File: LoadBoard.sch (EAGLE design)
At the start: 76 parts, among them IC1 7805TV, IC2 LM358D, IC3 MCP23S17SO, Q1 IRFZ44N, Q2 16MHz, T1 BC817, U1 ATMEGA328P_TQFP, U2 MAX232SOIC16

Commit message: Added second MosFET Stage and Temperature  Sensing
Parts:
- added ENCODER, JP3: (no value), SparkFun-Connectors:M04POLAR
- added FAN_CTRL, VLOAD_ATT: TPB1,27, testpad:TPB1,27
- added H5, H6: 3MM, holes:MOUNT-PAD-ROUND3.0
- added KK3: SK104-PAD, heatsink:SK104-PAD
- added LED1, LED2: (no value), led:LEDB155
- added Q3: IRFZ44N, OwnStuff:IRFZ44N
- added R14, R15, R16: 100, rcl:R-EU_R1206
- added R17, R18: 4k7, rcl:R-EU_M1206
- added RST_EN: (no value), pinhead:PINHD-1X2
- added U$7, U$8: DS18B20, OwnStuff:DS18B20
- KK1: value SK129 -> SK104-PAD; device heatsink:SK129 -> heatsink:SK104-PAD
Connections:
- new net GNDIO: JP3.1, S1.C, S1.SW-
- new net LED1: R14.1, U1.PC4(ADC4/SDA)
- new net LED2: R15.1, U1.PC5(ADC5/SCL)
- new net N$43: LED1.A, R14.2
- new net N$44: LED2.A, R15.2
- new net N$45: JP3.4, S1.SW+
- new net N$46: JP3.3, S1.A
- new net N$47: Q3.G, R16.2
- new net N$49: JP3.2, S1.B
- new net RST_EN: C12.2, RST_EN.1
- new net TH1: R18.2, U$7.DQ, U1.PC0(ADC0)
- new net TH2: R17.2, U$8.DQ, U1.PC1(ADC1)
- net +12V: now also FAN.2; no longer FAN.1
- net BTN_A: now also U1.PD4(XCK/T0); no longer U1.PD3(INT1)
- net BTN_B: now also U1.PD3(INT1); no longer U1.PD4(XCK/T0)
- net ENC_A: now also ENCODER.3; no longer S1.A
- net ENC_B: now also ENCODER.2; no longer S1.B
- net ENC_BTN: now also ENCODER.4; no longer S1.SW+
- net FAN: now also FAN_CTRL.TP
- net GND: now also ENCODER.1, LED1.C, LED2.C, U$7.GND, U$8.GND; no longer S1.C, S1.SW-
- net LOAD+: now also Q3.D
- net N$10: now also R16.1
- net N$12: now also DTR_IN.TP; no longer RX_IN.TP
- net N$13: now also RX_IN.TP; no longer DTR_IN.TP
- net N$26: now also PWR_SWITCH.2; no longer PWR_SWITCH.1
- net N$35: now also U$6.CS2; no longer U$6.DI
- net N$36: now also U$6.CS1; no longer U$6.RW
- net N$38: now also U$6.RW; no longer U$6.CS1
- net N$39: now also U$6.DI; no longer U$6.CS2
- net N$41: now also PWR_SWITCH.1; no longer PWR_SWITCH.2
- net N$5: now also FAN.1; no longer FAN.2
- net N$7: now also RST_EN.2; no longer C12.2
- net VCC: now also R17.1, R18.1, U$7.VDD, U$8.VDD
- net VLOAD_ATT: now also VLOAD_ATT.TP
- net VLOAD_DROP: now also Q3.S, U1.PC2(ADC2)
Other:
- moved on the sheet: C12, C14, C15, C16, C17, C18, C6, C7, DTR_IN, FAN, KK2, Q2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

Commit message: added second fan controller
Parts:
- removed FAN: (no value), SparkFun-Connectors:M02POLAR
- removed FAN_CTRL: TPB1,27, testpad:TPB1,27
- added D3: BAS16J, diode:DIODE-SOD323-W
- added FAN1, FAN2: TPB1,27, testpad:TPB1,27
- added FAN1_CONN, FAN2_CONN: (no value), SparkFun-Connectors:M02POLAR
- added R19: 100, rcl:R-EU_R1206
- added T2: BC817, transistor:BC817-NPN-SOT23-BEC
- added U$10: LM2569, OwnStuff:LM2569
- added U$9: IRLML2502, GeekAmmo:N-CHANNEL-MOSFET-BSS138
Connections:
- removed net FAN: FAN_CTRL.TP, R6.1, U1.PD2(INT0)
- new net FAN1: FAN1.TP, R6.1, U1.PD2(INT0)
- new net FAN2: FAN2.TP, R19.1, U1.PB0(ICP)
- new net N$42: T2.E, U$9.G
- new net N$48: R19.2, T2.B
- new net N$50: D3.A, FAN2_CONN.1, U$9.D
- net +12V: now also D3.C, FAN1_CONN.2, FAN2_CONN.2, T1.C, T2.C, U$10.IN+; no longer FAN.2
- net GND: now also U$10.IN-, U$10.OUT-, U$9.S
- net N$5: now also FAN1_CONN.1; no longer FAN.1, T1.C
- net VCC: now also U$10.OUT+
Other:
- note added: "Encoder Riser Board & Input"
- note added: "Frontpanel I/O"
- note added: "Optional LM2569 Equip EITHER with 7805 OR LM2569"
- note added: "Temperature Sensing"
- note removed: "Input"
- moved on the sheet: +12V, +5V, C1, C14, C15, C16, C17, C18, C2, C3, C4, C5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

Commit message: worked on silkscreen for passives
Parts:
- C3: value 24µ -> 100µ; device rcl:CPOL-EU150CLZ-0810 -> rcl:CPOL-EU175TMP-0808
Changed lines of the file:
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@@
 <part name="C1" library="rcl" deviceset="C-EU" device="C1206K" value="100n"/>
 <part name="C2" library="rcl" deviceset="C-EU" device="C1206K" value="100n"/>
-<part name="C3" library="rcl" deviceset="CPOL-EU" device="150CLZ-0810" value="24µ"/>
+<part name="C3" library="rcl" deviceset="CPOL-EU" device="175TMP-0808" value="100µ"/>
 <part name="GND2" library="supply1" deviceset="GND" device=""/>
 <part name="P+4" library="supply1" deviceset="VCC" device=""/>

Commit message: added silkscreen information to bottom
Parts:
- removed PWR: BLUE, SparkFun-LED:LED0603
- removed U$7, U$8: DS18B20, OwnStuff:DS18B20
- added IC8, IC9: DS18B20, OwnStuff:DS18B20
- added LED3: (no value), led:LEDB155
- added LED4: BLUE, SparkFun-LED:LED0603
- added R20: 100, rcl:R-EU_R1206
- Q1, Q3: value IRFZ44N -> IRF3710
- U$10: value LM2569 -> LM2569NO_OUTLINE; device OwnStuff:LM2569 -> OwnStuff:LM2569NO_OUTLINE
- renumbered ENCODER to JP4, RST_EN to JP5, RXI to LED5, TXI to LED6, U$1 to IC6, U$2 to IC7, U$4 to U4, U$9 to U9, U1 to IC4, U2 to IC5
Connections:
- new net N$51: LED3.A, R20.2
- net GND: now also IC8.GND, IC9.GND, LED3.C, LED4.C; no longer PWR.C, U$7.GND, U$8.GND
- net N$20: now also LED4.A; no longer PWR.A
- net TH1: now also IC8.DQ; no longer U$7.DQ
- net TH2: now also IC9.DQ; no longer U$8.DQ
- net VCC: now also IC8.VDD, IC9.VDD, R20.1; no longer U$7.VDD, U$8.VDD
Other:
- moved on the sheet: +12V, +5V, C1, C2, C3, D2, IC1, JP1, PWR_SWITCH, R10, R17, R18

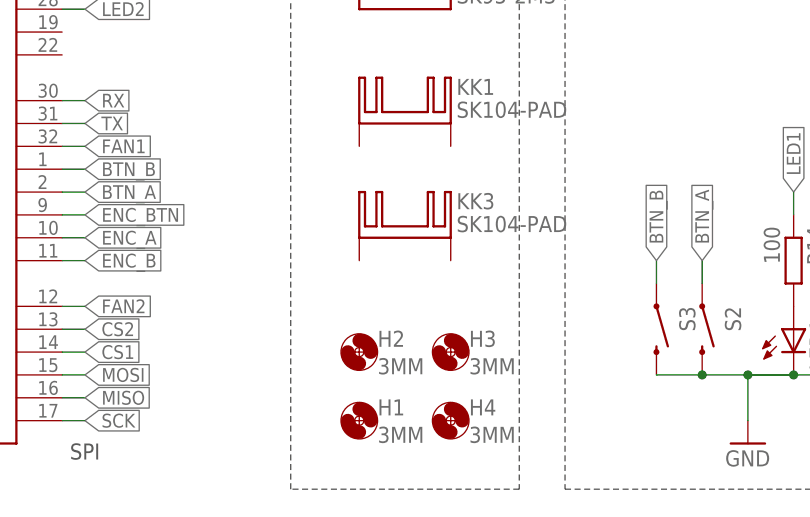
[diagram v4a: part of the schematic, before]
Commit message: added fiducials to the board
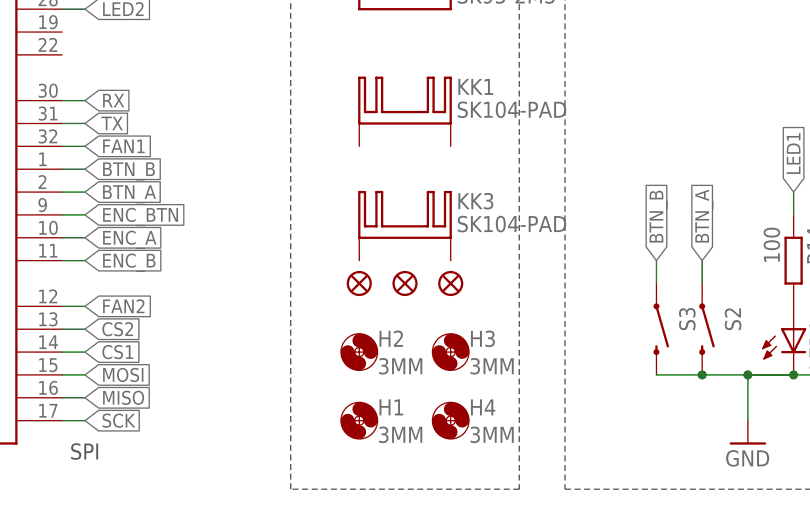
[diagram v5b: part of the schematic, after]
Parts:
- added FID1, FID2, FID3: FIDUCIAL1X2, SparkFun-Aesthetics:FIDUCIAL1X2
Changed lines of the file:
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@@
 <part name="LED3" library="led" deviceset="LED" device="B155"/>
 <part name="R20" library="rcl" deviceset="R-EU_" device="R1206" value="100"/>
+<part name="FID1" library="SparkFun-Aesthetics" deviceset="FIDUCIAL" device="1X2" value="FIDUCIAL1X2"/>
+<part name="FID2" library="SparkFun-Aesthetics" deviceset="FIDUCIAL" device="1X2" value="FIDUCIAL1X2"/>
+<part name="FID3" library="SparkFun-Aesthetics" deviceset="FIDUCIAL" device="1X2" value="FIDUCIAL1X2"/>
 </parts>
 <sheets>
@@
 <instance part="LED3" gate="G$1" x="-15.24" y="25.4"/>
 <instance part="R20" gate="G$1" x="-15.24" y="33.02" rot="R270"/>
+<instance part="FID1" gate="G$1" x="-152.4" y="-78.74"/>
+<instance part="FID2" gate="G$1" x="-142.24" y="-78.74"/>
+<instance part="FID3" gate="G$1" x="-147.32" y="-78.74"/>
 </instances>
 <busses>
